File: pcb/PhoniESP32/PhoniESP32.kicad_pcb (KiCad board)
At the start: 4 copper layers, 57.4 x 36.4 mm, 73 parts, among them J1 Connector, USB-TYPE-C-16P, J2 Conn_Battery, J3 Conn_Buttons, J4 Conn_01x08_Pin, J5 Screw_Terminal_01x02, SW1 SK12D07VG5, U1 TPS631000DRLR, U2 MAX98357AETE+T, U3 ESP32-C6-MINI-1-N4, U4 SPH0645LM4H-1-8_C19272537, U5 BQ24073RGTR

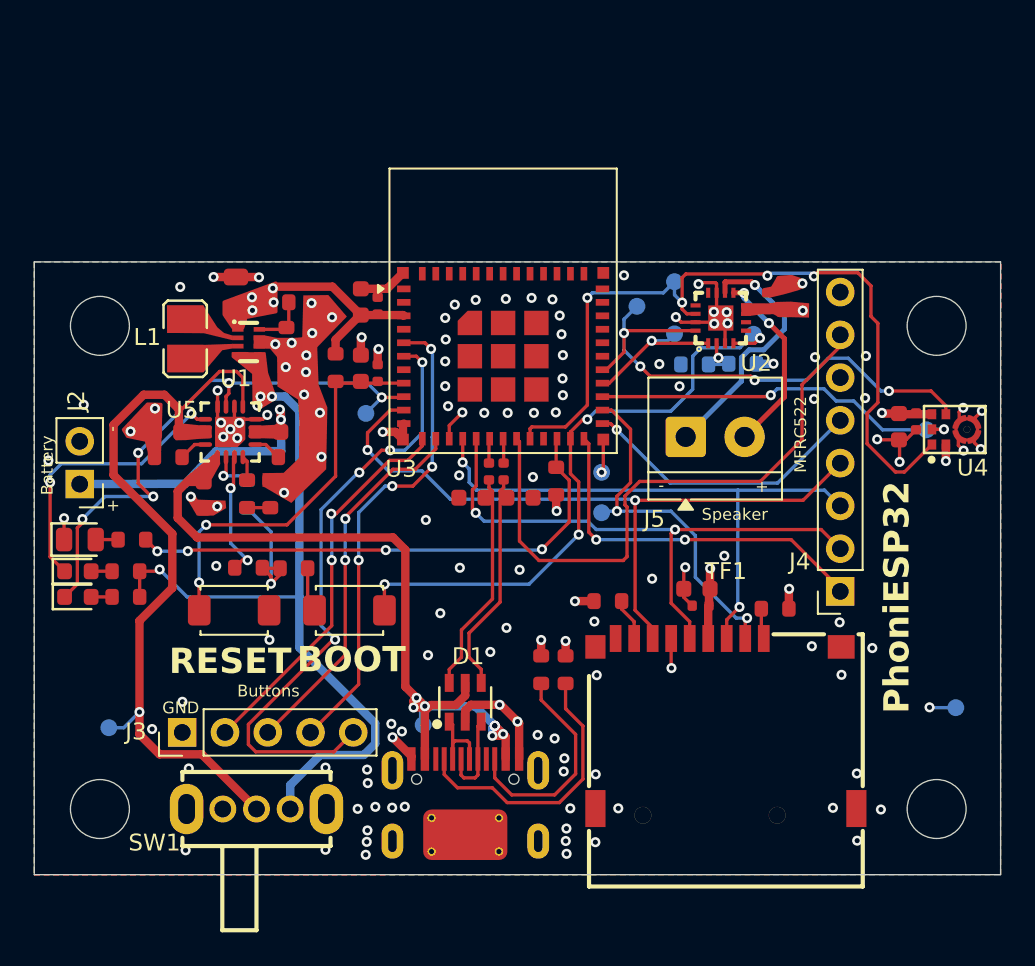
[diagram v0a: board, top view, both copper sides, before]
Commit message: chore(pcb): switch from PCB antenna to connector
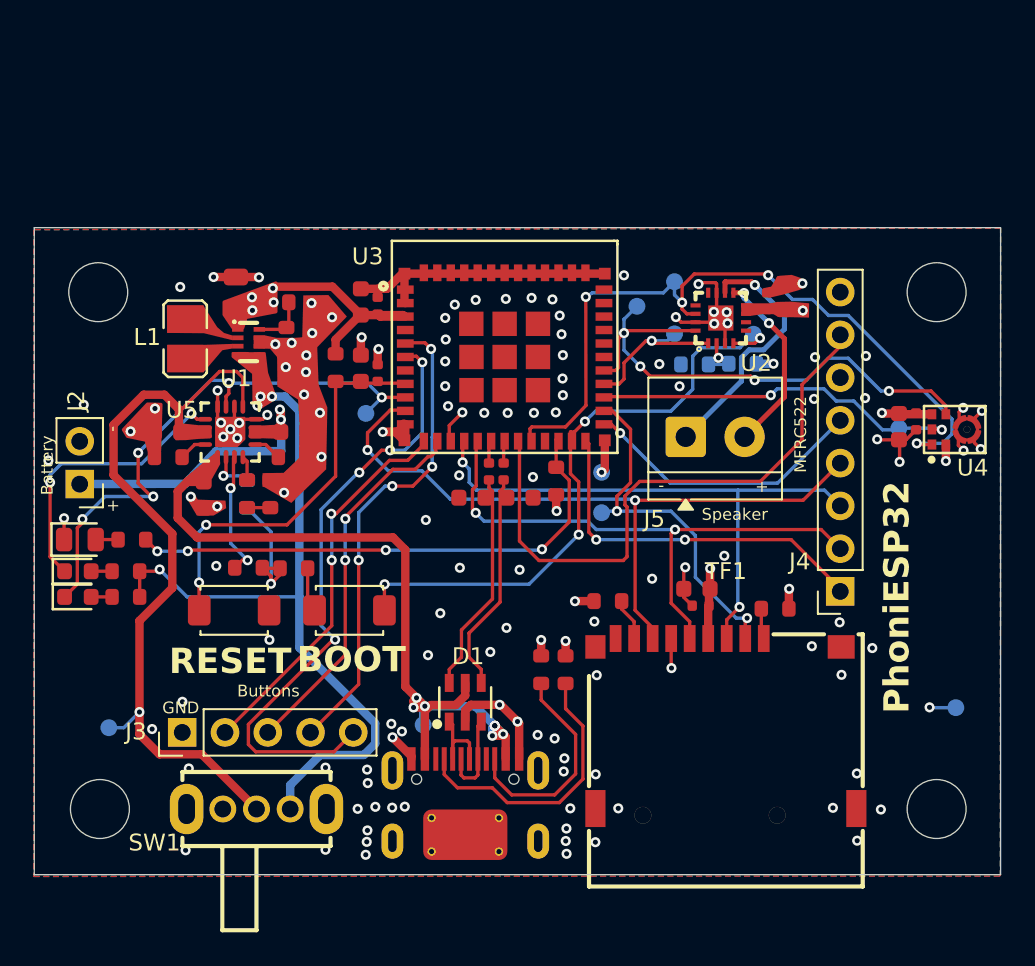
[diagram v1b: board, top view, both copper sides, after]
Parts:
- U3: value ESP32-C6-MINI-1-N4 -> ESP32-C6-MINI-1U-H4; footprint RF_Module:ESP32-C6-MINI-1 -> JLCPCB:WIFIM-SMD_61P-L13.2-W12.5-P0.80
- moved REF** 2.00 mm to (124.9, 88.2)
- moved REF** 2.00 mm to (174.7, 88.2)
- moved TP8 1.64 mm to (172.5, 96.3)
- moved U3 0.10 mm to (149.0, 92.0)
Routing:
- net GND: track 76.0 -> 94.2 mm
- net /I2S_WS: track 48.0 -> 44.7 mm
- net +3.3V: track 32.8 -> 34.5 mm
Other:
- board size 57.4 x 36.4 mm -> 57.4 x 38.4 mm

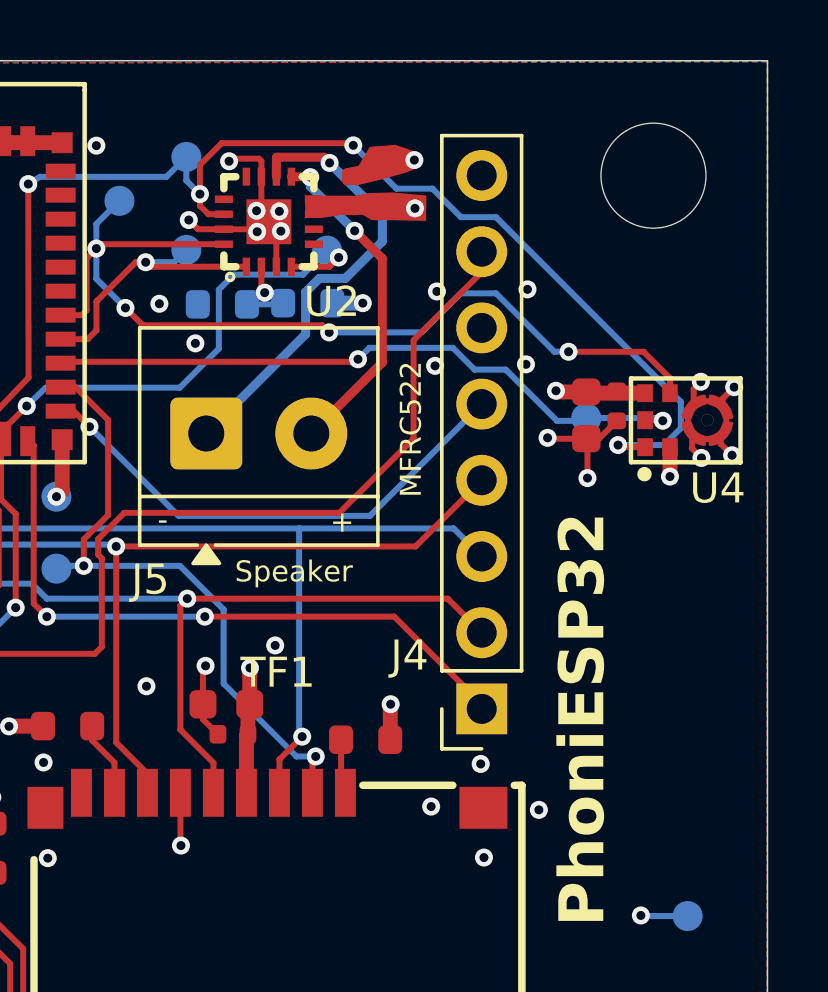
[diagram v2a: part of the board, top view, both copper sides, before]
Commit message: fix(pcb): swap pin connector for header
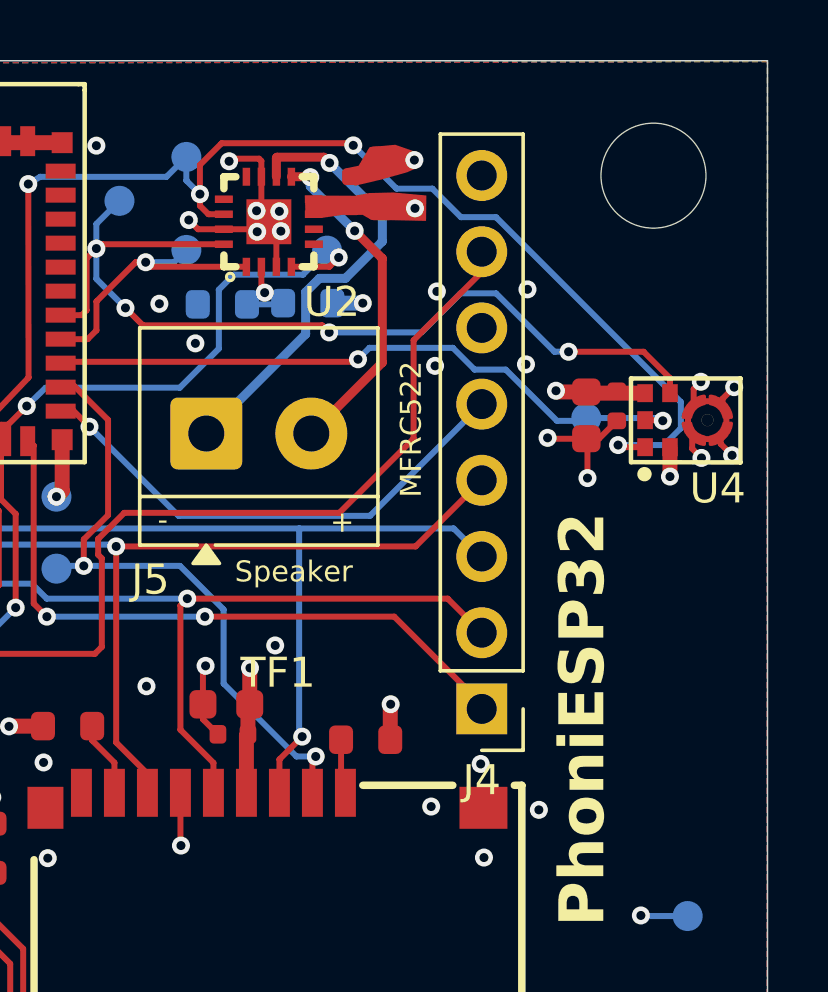
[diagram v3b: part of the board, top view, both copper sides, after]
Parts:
- J4: footprint Connector_PinSocket_2.54mm:PinSocket_1x08_P2.54mm_Vertical -> Connector_PinHeader_2.54mm:PinHeader_1x08_P2.54mm_Vertical

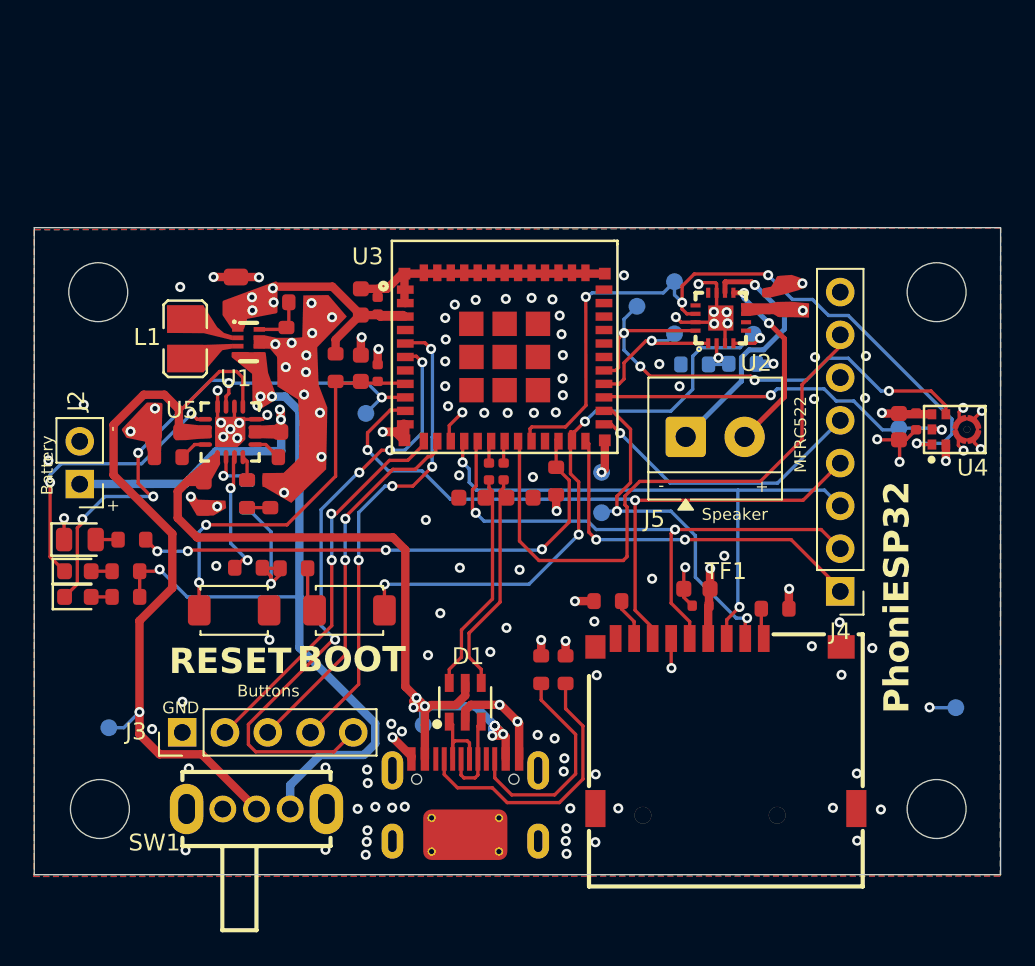
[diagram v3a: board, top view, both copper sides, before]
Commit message: feat(pcb): version for hand soldering
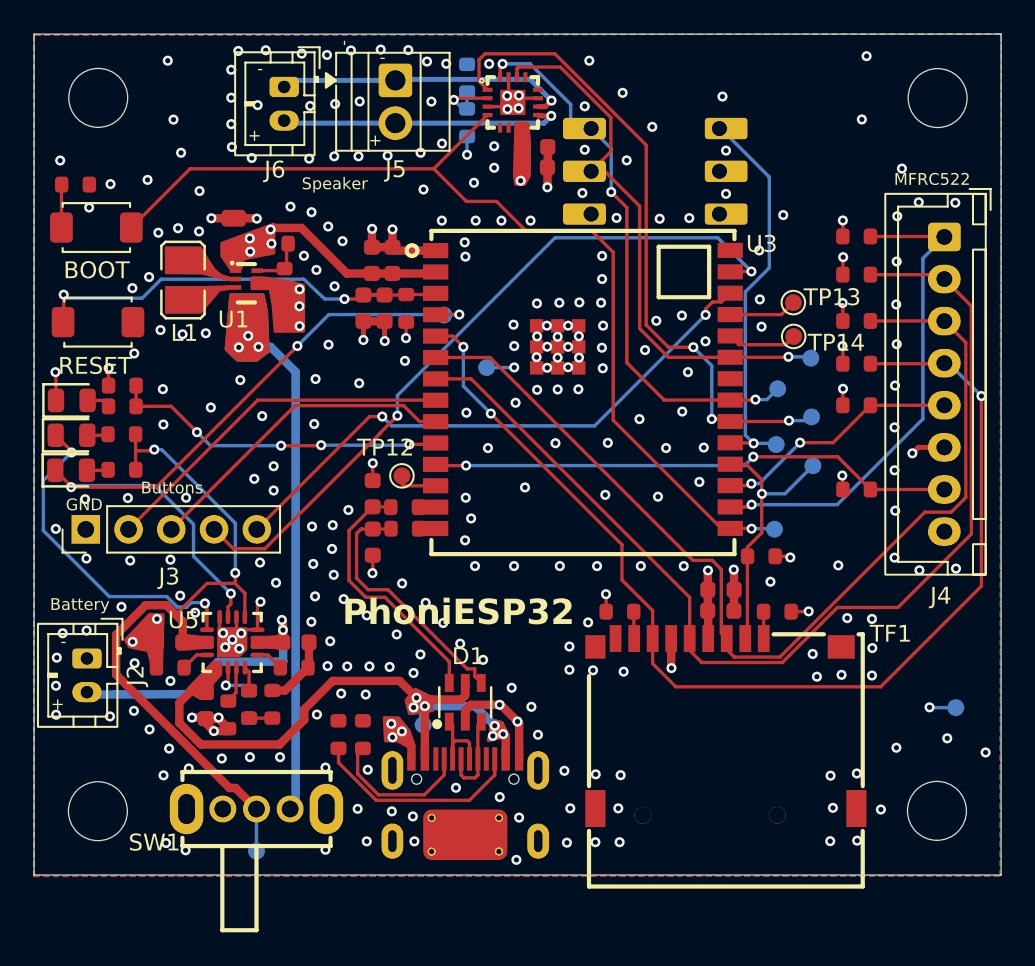
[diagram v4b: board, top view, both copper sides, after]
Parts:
- removed C14: 100nF, PCM_JLCPCB:C_0402
- removed C15: 200pF, PCM_JLCPCB:C_0603
- added J6: Conn_01x02_Pin, Connector_JST:JST_PH_B2B-PH-K_1x02_P2.00mm_Vertical, F.Cu at (135.9, 76.0)
- added R23: 47kΩ, PCM_JLCPCB:R_0603, F.Cu at (164.3, 103.9)
- added R24: 47kΩ, PCM_JLCPCB:R_0603, F.Cu at (169.9, 89.9)
- added R25: 47kΩ, PCM_JLCPCB:R_0603, F.Cu at (169.9, 87.2)
- added R26: 47kΩ, PCM_JLCPCB:R_0603, F.Cu at (169.9, 92.5)
- added R27: 47kΩ, PCM_JLCPCB:R_0603, F.Cu at (169.9, 94.9)
- added R28: 47kΩ, PCM_JLCPCB:R_0603, F.Cu at (169.9, 84.9)
- added R29: 47kΩ, PCM_JLCPCB:R_0603, F.Cu at (169.9, 99.9)
- added TP12: TestPoint, TestPoint:TestPoint_Pad_D1.0mm, F.Cu at (142.9, 99.1)
- added TP13: TestPoint, TestPoint:TestPoint_Pad_D1.0mm, F.Cu at (166.2, 88.8)
- added TP14: TestPoint, TestPoint:TestPoint_Pad_D1.0mm, F.Cu at (166.2, 90.8)
- C10, C13, C7, C9: footprint PCM_JLCPCB:C_0402 -> PCM_JLCPCB:C_0603
- D2, D3: footprint PCM_JLCPCB:D_0603 -> PCM_JLCPCB:D_0805
- J2: footprint Connector_PinHeader_2.54mm:PinHeader_1x02_P2.54mm_Vertical -> Connector_JST:JST_PH_B2B-PH-K_1x02_P2.00mm_Vertical
- J4: footprint Connector_PinHeader_2.54mm:PinHeader_1x08_P2.54mm_Vertical -> Connector_JST:JST_XH_B8B-XH-A_1x08_P2.50mm_Vertical
- J5: footprint TerminalBlock_4Ucon:TerminalBlock_4Ucon_1x02_P3.50mm_Horizontal -> TerminalBlock:TerminalBlock_Xinya_XY308-2.54-2P_1x02_P2.54mm_Horizontal
- R10, R11: footprint PCM_JLCPCB:R_0402 -> PCM_JLCPCB:R_0603
- R13: value 150Ω -> 200Ω
- R8: value 91kΩ -> 510kΩ
- R9: value 510kΩ -> 91kΩ
- U3: value ESP32-C6-MINI-1U-H4 -> ESP32-C6-WROOM-1U-N4; footprint JLCPCB:WIFIM-SMD_61P-L13.2-W12.5-P0.80 -> JLCPCB:WIFIM-SMD_28P-L19.2-W18.0-P1.27-TL
- U4: value SPH0645LM4H-1-8_C19272537 -> INMP411_MODULE; footprint JLCPCB:MIC-SMD_6P-L3.5-W2.7-P0.90-BL -> JLCPCB:INMP411_MODULE; moved to B.Cu
- moved J5 27.3 mm to (142.6, 75.6), turned to -90 degrees
- moved S2 27.3 mm to (124.8, 84.4)
- moved R18 26.4 mm to (126.3, 93.8), turned to 0 degrees
- moved R16 26.2 mm to (123.5, 81.8), turned to 180 degrees
- moved U4 23.4 mm to (158.0, 81.0), turned to 180 degrees
- moved J4 21.9 mm to (175.2, 84.9), turned to -90 degrees
- moved R21 21.7 mm to (146.8, 78.1), turned to 90 degrees
- moved R22 21.7 mm to (146.8, 75.5), turned to 90 degrees
- moved S1 18.9 mm to (124.9, 90.0)
- moved U2 17.8 mm to (149.5, 76.9), turned to -90 degrees
- moved C12 16.7 mm to (150.8, 80.8), turned to 0 degrees
- moved C13 16.6 mm to (150.8, 79.6), turned to 0 degrees
- moved J3 13.4 mm to (124.2, 102.3)
- moved TP11 12.9 mm to (167.3, 98.5)
- moved R2 12.6 mm to (139.2, 114.5)
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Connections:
- C2 pad 1: GND -> /Power/BAT+
- C2 pad 2: Net-(J2-Pin_1) -> GND
- C3 pad 1: Net-(U5-EN2) -> /Power/VIN
- C4 pad 1: +5V -> /Power/VIN_SW
- J2 pad 1: Net-(J2-Pin_1) -> GND
- J2 pad 2: GND -> /Power/BAT+
- R6 pad 1: +5V -> /Power/VIN
- R7 pad 1: +5V -> /Power/VIN
- R8 pad 1: Net-(U1-FB) -> +3.3V
- R8 pad 2: GND -> Net-(U1-FB)
- R9 pad 1: +3.3V -> Net-(U1-FB)
- R9 pad 2: Net-(U1-FB) -> GND
- SW1 pad 2: Net-(U5-EN2) -> /Power/VIN
- SW1 pad 3: +5V -> /Power/VIN_SW
- TP5 pad 1: Net-(U5-EN2) -> /Power/VIN
- U1 pad 4: +5V -> /Power/VIN_SW
- U1 pad 5: +5V -> /Power/VIN_SW
- U3 pad 10: /SPI_MISO -> Net-(U3-IO8)
- U3 pad 11: GND -> /RFID_EN
- U3 pad 12: /BTN_PLAY -> Net-(U3-IO11)
- U3 pad 13: /BTN_NEXT -> Net-(U3-IO12)
- U3 pad 14: GND -> Net-(U3-IO13)
- U3 pad 15: /SPI_MOSI -> /AUDIO_EN
- U3 pad 16: /SPI_SCK -> /RFID_CS
- U3 pad 17: Net-(U3-IO12) -> /RFID_IRQ
- U3 pad 18: Net-(U3-IO13) -> /SD_CS
- U3 pad 19: /RFID_EN -> /I2S_DIN
- U3 pad 2: GND -> +3.3V
- U3 pad 20: /I2S_WS -> /I2S_DOUT
- U3 pad 21: unconnected-(U3-NC-Pad21) -> /I2S_BCLK
- U3 pad 22: Net-(U3-IO8) -> unconnected-(U3-NC-Pad22)
- U3 pad 23: /AUDIO_EN -> /I2S_WS
- U3 pad 24: /RFID_CS -> Net-(U3-RXD0)
- U3 pad 25: /RFID_IRQ -> Net-(U3-TXD0)
- U3 pad 26: /SD_CS -> /BTN_VOL_UP
- U3 pad 27: /I2S_DIN -> /BTN_VOL_DOWN
- U3 pad 28: /I2S_DOUT -> GND
- U3 pad 29: /I2S_BCLK -> GND
- U3 pad 3: +3.3V -> /ESP_EN
- U3 pad 4: unconnected-(U3-NC-Pad4) -> /CHARGER
- U3 pad 5: /BTN_VOL_DOWN -> /SPI_MISO
- U3 pad 6: /BTN_VOL_UP -> /SPI_MOSI
- U3 pad 7: unconnected-(U3-NC-Pad7) -> /SPI_SCK
- U3 pad 8: /ESP_EN -> /BTN_PLAY
- U3 pad 9: /CHARGER -> /BTN_NEXT
- U4 pad 1: /I2S_WS -> /I2S_BCLK
- U4 pad 2: +3.3V -> /I2S_WS
- U4 pad 3: GND -> unconnected-(U4-L/R-Pad3)
- U4 pad 4: /I2S_BCLK -> /I2S_DIN
- U4 pad 6: /I2S_DIN -> GND
- U5 pad 10: Net-(U5-EN2) -> /Power/VIN
- U5 pad 11: Net-(U5-EN2) -> /Power/VIN
- U5 pad 2: Net-(J2-Pin_1) -> /Power/BAT+
- U5 pad 3: Net-(J2-Pin_1) -> /Power/BAT+
- U5 pad 5: Net-(U5-EN2) -> /Power/VIN
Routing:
- net +5V: track 50.5 -> 0.00 mm, vias 4 -> 0
- net Net-(U5-EN2): track 47.3 -> 0.00 mm, vias 1 -> 0
- net /Power/VIN: track 0.00 -> 42.8 mm, vias 0 -> 2
- net GND: track 94.2 -> 56.6 mm, vias 132 -> 300
- net /SPI_SCK: track 34.1 -> 64.1 mm, vias 2 -> 0
- net /I2S_DOUT: track 9.40 -> 39.3 mm, vias 1 -> 3
- net /Power/VIN_SW: track 0.00 -> 28.9 mm, vias 0 -> 3
- net /SPI_MOSI: track 34.6 -> 60.8 mm, vias 2 -> 0
- net /SPI_MISO: track 42.6 -> 66.7 mm, vias 2 -> 3
- net /AUDIO_EN: track 37.4 -> 58.9 mm, vias 4 -> 1
- net Net-(J2-Pin_1): track 18.8 -> 0.00 mm, vias 2 -> 0
- net /Power/BAT+: track 0.00 -> 18.8 mm, vias 0 -> 2
- net /BTN_VOL_DOWN: track 28.5 -> 42.9 mm, vias 4 -> 2
- net VBUS: track 46.2 -> 34.0 mm, vias 7 -> 6
- net /I2S_WS: track 44.7 -> 33.0 mm, vias 4 -> 1
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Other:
- board size 57.4 x 38.4 mm -> 57.4 x 49.9 mm
- board text removed: "JLCJLCJLCJLC"

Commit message: feat(pcb): add labels for basic components
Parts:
- C1, C10, C11, C12, C13, C16, C17, C2, C3, C4, C6, C7, C8, C9: footprint PCM_JLCPCB:C_0603 -> JLCPCB:C_0603_Label
- R1: value 5.1kΩ -> 2x5.1kΩ; footprint PCM_JLCPCB:R_0603 -> JLCPCB:R_0603_Label
- R10, R11, R12, R13, R14, R15, R16, R17, R18, R19, R2, R20, R21, R22, R23, R24, R25, R26, R27, R28, R29, R3, R5, R6, R7, R8, R9: footprint PCM_JLCPCB:R_0603 -> JLCPCB:R_0603_Label
- R4: value 1.5kΩ -> 2x1.5kΩ; footprint PCM_JLCPCB:R_0603 -> JLCPCB:R_0603_Label
